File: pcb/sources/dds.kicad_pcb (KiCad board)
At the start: 2 copper layers, 82.3 x 64.5 mm, 11 parts, among them P1 CONN_01X02, P2 CONN_01X02, SW1 Control, U1 AD9850_BreakOut, U2 ArduinoProClone

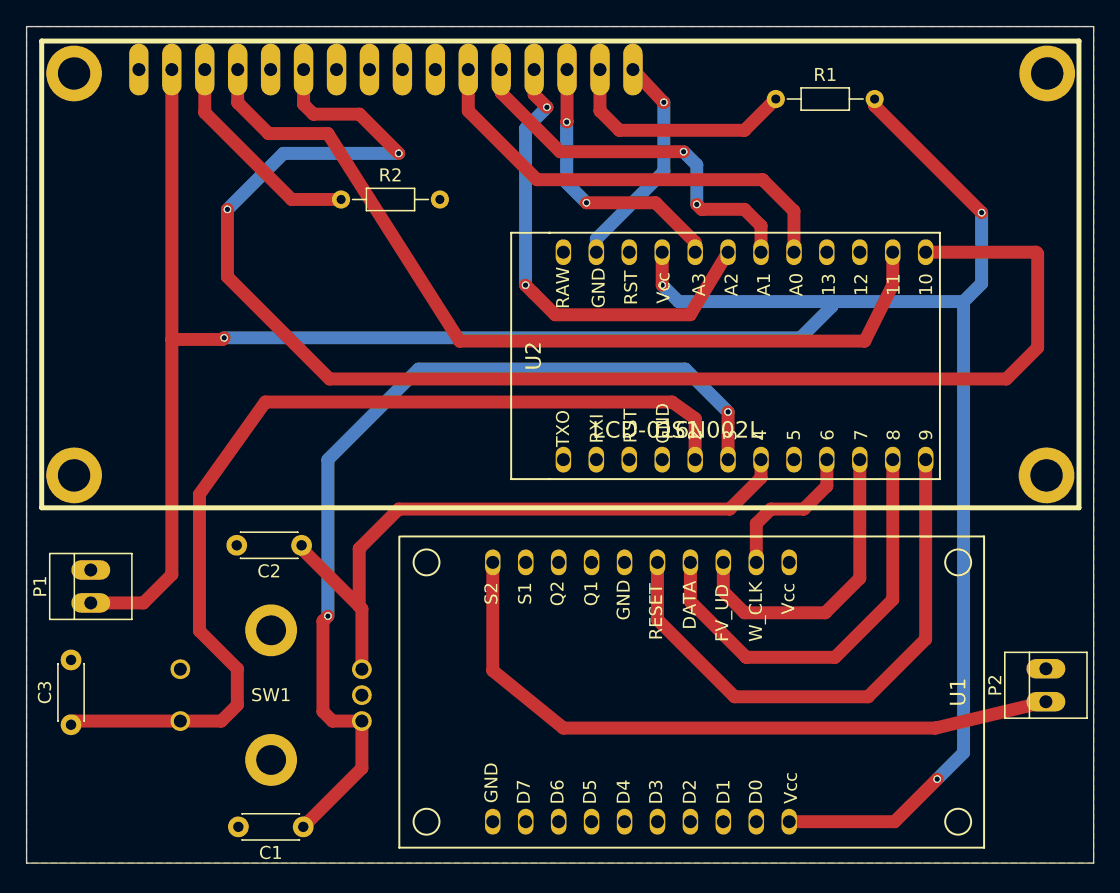
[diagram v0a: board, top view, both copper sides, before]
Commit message: Minor tracks re-route in front layer
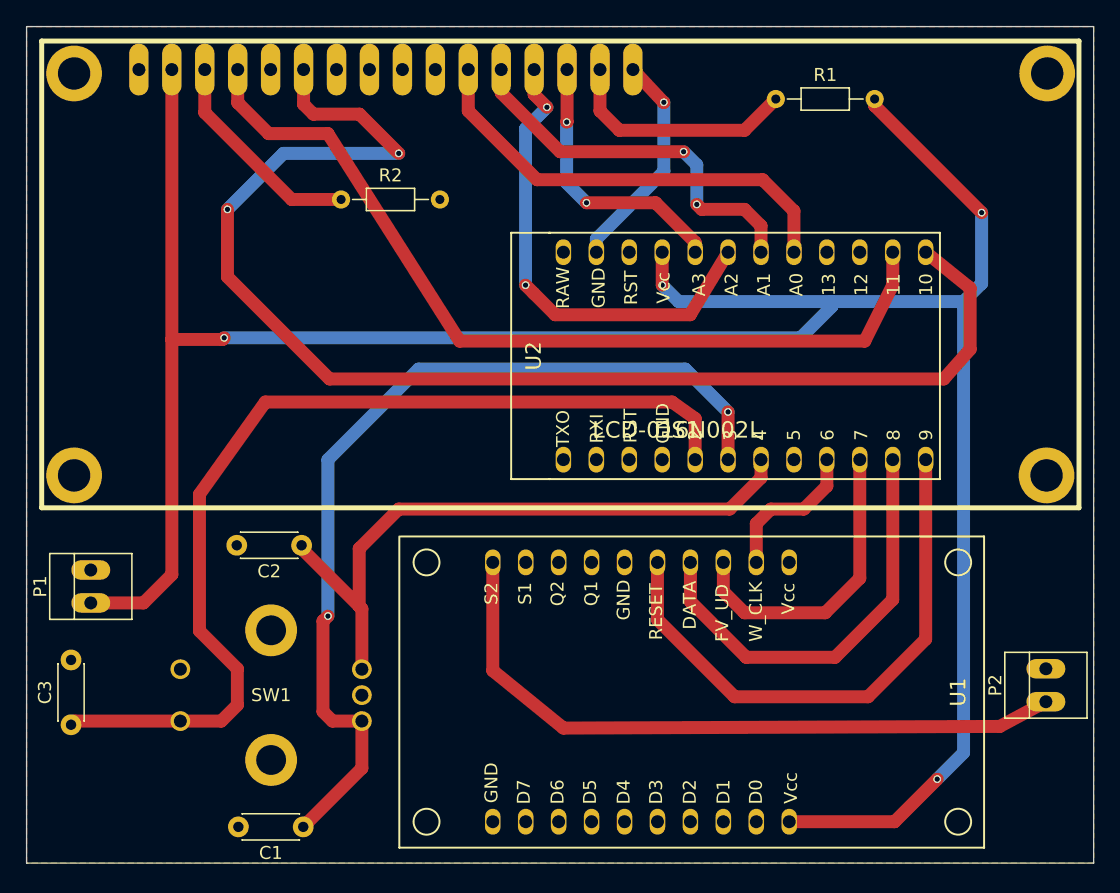
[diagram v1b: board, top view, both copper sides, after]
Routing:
- net Net-(DS1-Pad6): track 114.5 -> 102.5 mm
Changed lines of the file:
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@@
   (layers
     (0 F.Cu signal)
-    (31 B.Cu signal)
+    (31 B.Cu signal hide)
     (32 B.Adhes user)
     (33 F.Adhes user)
@@
   (segment (start 171.958 91.44) (end 140.716 91.44) (width 1) (layer F.Cu) (net 7))
   (segment (start 174.117 87.122) (end 171.958 91.44) (width 1) (layer F.Cu) (net 7))
-  (segment (start 176.657 84.583) (end 185.167 84.583) (width 1) (layer F.Cu) (net 8))
+  (segment (start 176.657 84.583) (end 179.959 87.249) (width 1) (layer F.Cu) (net 8))
   (segment (start 128.67894 73.17994) (end 128.67894 70.4977) (width 1) (layer F.Cu) (net 8))
   (segment (start 129.436998 73.937998) (end 128.67894 73.17994) (width 1) (layer F.Cu) (net 8))
@@
   (segment (start 122.809 86.487) (end 122.809 81.28) (width 1) (layer F.Cu) (net 8))
   (segment (start 130.683 94.361) (end 122.809 86.487) (width 1) (layer F.Cu) (net 8))
-  (segment (start 182.88 94.361) (end 130.683 94.361) (width 1) (layer F.Cu) (net 8))
-  (segment (start 185.293 91.948) (end 182.88 94.361) (width 1) (layer F.Cu) (net 8))
-  (segment (start 185.293 84.709) (end 185.293 91.948) (width 1) (layer F.Cu) (net 8))
-  (segment (start 185.167 84.583) (end 185.293 84.709) (width 1) (layer F.Cu) (net 8))
+  (segment (start 178.054 94.361) (end 130.683 94.361) (width 1) (layer F.Cu) (net 8))
+  (segment (start 180.086 92.075) (end 178.054 94.361) (width 1) (layer F.Cu) (net 8))
+  (segment (start 180.085 87.375) (end 180.086 92.075) (width 1) (layer F.Cu) (net 8))
+  (segment (start 179.959 87.249) (end 180.085 87.375) (width 1) (layer F.Cu) (net 8))
   (segment (start 141.37894 70.4977) (end 141.37894 73.68794) (width 1) (layer F.Cu) (net 13))
   (segment (start 166.497 81.407) (end 166.497 84.583) (width 1) (layer F.Cu) (net 13))
@@
   (segment (start 151.53894 73.68794) (end 153.035 75.184) (width 1) (layer F.Cu) (net 17))
   (segment (start 143.272 108.507) (end 143.272 116.856) (width 1) (layer F.Cu) (net 18))
-  (segment (start 177.419 121.285) (end 185.928 119.253) (width 1) (layer F.Cu) (net 18))
-  (segment (start 148.717 121.285) (end 177.419 121.285) (width 1) (layer F.Cu) (net 18))
+  (segment (start 182.372 121.158) (end 185.928 119.253) (width 1) (layer F.Cu) (net 18))
+  (segment (start 148.717 121.285) (end 182.372 121.158) (width 1) (layer F.Cu) (net 18))
   (segment (start 143.272 116.856) (end 148.717 121.285) (width 1) (layer F.Cu) (net 18))
   (segment (start 169.037 100.583) (end 169.037 102.616) (width 1) (layer F.Cu) (net 20))
